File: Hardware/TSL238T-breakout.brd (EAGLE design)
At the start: 15 x 15 mm, 5 parts, among them J1 CONN_42.54_NOSILK

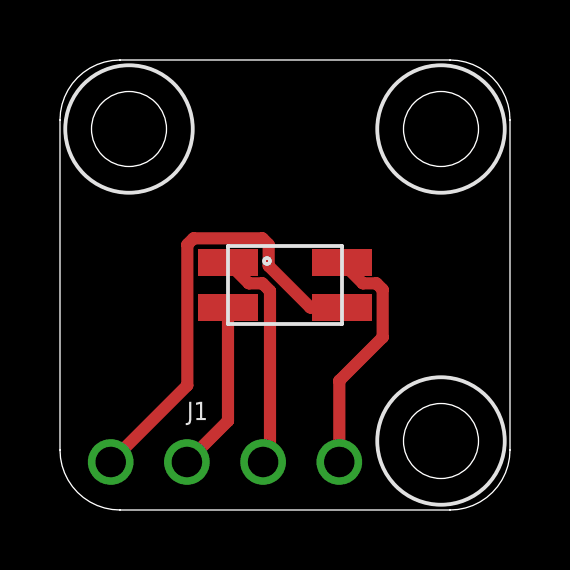
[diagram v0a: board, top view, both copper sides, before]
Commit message: Updated breakouts and main board, schematic v0.1 updates
Updated schematic for main unit to v0.1, incorporating updates from testing of v0.0 unit
Minor updates to breakout boards, adding passives and updating components
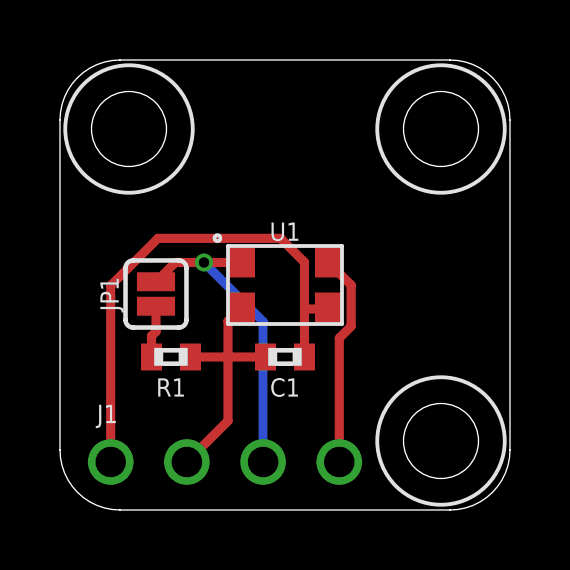
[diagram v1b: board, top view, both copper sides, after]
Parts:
- removed U$1: TSL238T, bschulz:TSL238T
- added C1: 0.1uF, bschulz_passives:C0402
- added JP1: JUMPER-SMT_2_NC_PASTE_SILK, SparkFun-Jumpers:SMT-JUMPER_2_NC_PASTE_SILK
- added R1: 10k, bschulz_passives:R0402
- added U1: TSL237T, bschulz:TSL237T
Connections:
- removed net OE: J1.3, U$1.OE_INV
- new net !OE: J1.3, JP1.2, U1.OE
- new net N$2: JP1.1, R1.2
- net GND: now also C1.2, R1.1, U1.GND; no longer U$1.GND
- net OUT: now also U1.OUT; no longer U$1.OUT
- net VDD: now also C1.1, U1.VDD; no longer U$1.VDD
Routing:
- net !OE: track 0.00 -> 10.6 mm, vias 0 -> 1
- net OE: track 7.59 -> 0.00 mm
- net GND: track 5.72 -> 8.40 mm
- net VDD: track 14.9 -> 17.3 mm
- net N$2: track 0.00 -> 1.76 mm
- net OUT: track 8.08 -> 7.13 mm
